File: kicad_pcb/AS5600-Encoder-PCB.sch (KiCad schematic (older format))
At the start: 12 parts, among them IC1 AS5600-ASOM, J1 Conn_01x04_Male, J2 Conn_01x04_Male

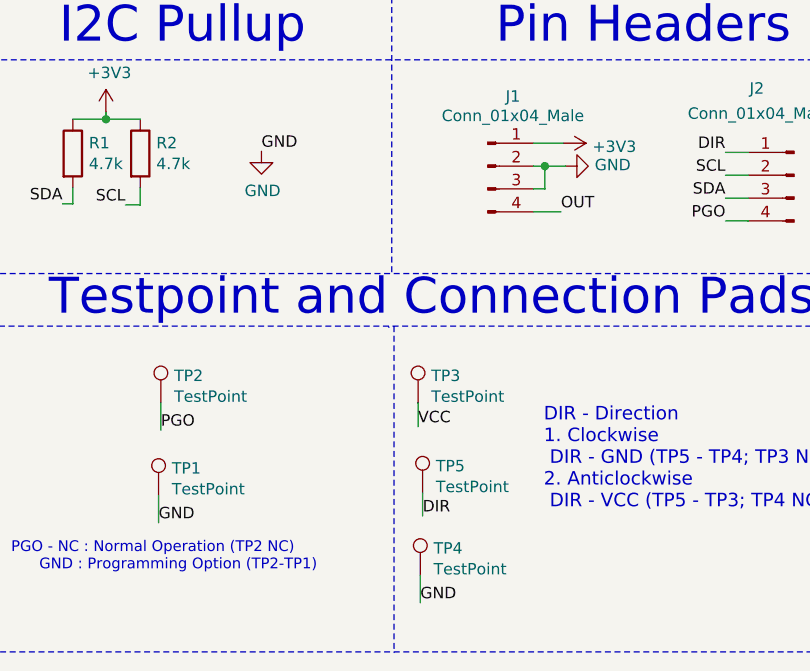
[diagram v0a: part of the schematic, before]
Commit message: Added SMD PCB for AS5600 Controller Board
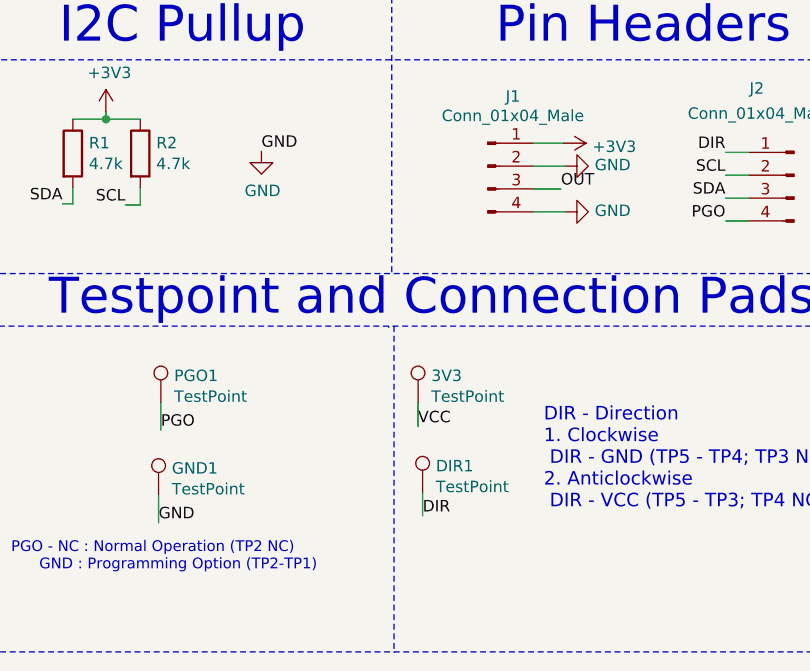
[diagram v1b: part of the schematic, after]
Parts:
- removed TP4: TestPoint, TestPoint:TestPoint_Pad_D2.5mm, symbol Connector:TestPoint
- C1: footprint Capacitor_THT:C_Disc_D5.0mm_W2.5mm_P5.00mm -> Capacitor_SMD:C_1206_3216Metric_Pad1.42x1.75mm_HandSolder
- C2: footprint Capacitor_THT:C_Radial_D6.3mm_H11.0mm_P2.50mm -> Capacitor_SMD:C_1206_3216Metric_Pad1.42x1.75mm_HandSolder
- R1, R2: footprint Resistor_THT:R_Axial_DIN0207_L6.3mm_D2.5mm_P10.16mm_Horizontal -> Resistor_SMD:R_1206_3216Metric_Pad1.42x1.75mm_HandSolder
- renumbered TP3 to 3V3, TP5 to DIR1, TP1 to GND1, TP2 to PGO1
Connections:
- net GND: now also J1.4 (Pin_4); no longer J1.3 (Pin_3)
- net OUT: now also J1.3 (Pin_3); no longer J1.4 (Pin_4)
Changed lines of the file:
@@
 F 0 "R1" H 3215 1246 50  0000 L CNN
 F 1 "4.7k" H 3215 1155 50  0000 L CNN
-F 2 "Resistor_THT:R_Axial_DIN0207_L6.3mm_D2.5mm_P10.16mm_Horizontal" V 3075 1200 50  0001 C CNN
+F 2 "Resistor_SMD:R_1206_3216Metric_Pad1.42x1.75mm_HandSolder" V 3075 1200 50  0001 C CNN
 F 3 "~" H 3145 1200 50  0001 C CNN
 	1    3145 1200
@@
 F 0 "R2" H 3510 1246 50  0000 L CNN
 F 1 "4.7k" H 3510 1155 50  0000 L CNN
-F 2 "Resistor_THT:R_Axial_DIN0207_L6.3mm_D2.5mm_P10.16mm_Horizontal" V 3370 1200 50  0001 C CNN
+F 2 "Resistor_SMD:R_1206_3216Metric_Pad1.42x1.75mm_HandSolder" V 3370 1200 50  0001 C CNN
 F 3 "~" H 3440 1200 50  0001 C CNN
 	1    3440 1200
@@
 F 0 "C1" H 885 2474 50  0000 R CNN
 F 1 "0.1uF" H 885 2565 50  0000 R CNN
-F 2 "Capacitor_THT:C_Disc_D5.0mm_W2.5mm_P5.00mm" H 1038 2370 50  0001 C CNN
+F 2 "Capacitor_SMD:C_1206_3216Metric_Pad1.42x1.75mm_HandSolder" H 1038 2370 50  0001 C CNN
 F 3 "~" H 1000 2520 50  0001 C CNN
 	1    1000 2520
@@
 F 0 "C2" H 1555 2566 50  0000 L CNN
 F 1 "10uF" H 1555 2475 50  0000 L CNN
-F 2 "Capacitor_THT:C_Radial_D6.3mm_H11.0mm_P2.50mm" H 1478 2370 50  0001 C CNN
+F 2 "Capacitor_SMD:C_1206_3216Metric_Pad1.42x1.75mm_HandSolder" H 1478 2370 50  0001 C CNN
 F 3 "~" H 1440 2520 50  0001 C CNN
 	1    1440 2520
@@
 	0    -1   -1   0
 $EndComp
-Text Label 5280 1455 0    50   ~ 0
+Text Label 5280 1355 0    50   ~ 0
 OUT
 $Comp
@@
 	5160 1155 5290 1155
 Wire Wire Line
-	5160 1455 5280 1455
-Wire Wire Line
-	5160 1255 5210 1255
-Wire Wire Line
-	5210 1255 5210 1355
-Wire Wire Line
-	5210 1355 5160 1355
-Wire Wire Line
-	5210 1255 5300 1255
-Connection ~ 5210 1255
-$Comp
-L Connector:TestPoint TP2
+	5160 1355 5280 1355
+$Comp
+L Connector:TestPoint PGO1
 U 1 1 61273AD3
 P 3530 2290
-F 0 "TP2" H 3588 2408 50  0000 L CNN
+F 0 "PGO1" H 3588 2408 50  0000 L CNN
 F 1 "TestPoint" H 3588 2317 50  0000 L CNN
 F 2 "TestPoint:TestPoint_Pad_D2.5mm" H 3730 2290 50  0001 C CNN
@@
 $EndComp
 $Comp
-L Connector:TestPoint TP3
+L Connector:TestPoint 3V3
 U 1 1 61274B3F
 P 4655 2290
-F 0 "TP3" H 4713 2408 50  0000 L CNN
+F 0 "3V3" H 4713 2408 50  0000 L CNN
 F 1 "TestPoint" H 4713 2317 50  0000 L CNN
 F 2 "TestPoint:TestPoint_Pad_D2.5mm" H 4855 2290 50  0001 C CNN
@@
 $EndComp
 $Comp
-L Connector:TestPoint TP5
+L Connector:TestPoint DIR1
 U 1 1 61275699
 P 4675 2685
-F 0 "TP5" H 4733 2803 50  0000 L CNN
+F 0 "DIR1" H 4733 2803 50  0000 L CNN
 F 1 "TestPoint" H 4733 2712 50  0000 L CNN
 F 2 "TestPoint:TestPoint_Pad_D2.5mm" H 4875 2685 50  0001 C CNN
 F 3 "~" H 4875 2685 50  0001 C CNN
 	1    4675 2685
-	1    0    0    -1
-$EndComp
-$Comp
-L Connector:TestPoint TP4
-U 1 1 61275D44
-P 4665 3045
-F 0 "TP4" H 4723 3163 50  0000 L CNN
-F 1 "TestPoint" H 4723 3072 50  0000 L CNN
-F 2 "TestPoint:TestPoint_Pad_D2.5mm" H 4865 3045 50  0001 C CNN
-F 3 "~" H 4865 3045 50  0001 C CNN
-	1    4665 3045
 	1    0    0    -1
 $EndComp
@@
 Text Label 1795 2370 0    50   ~ 0
 VCC
-Text Label 4665 3165 0    50   ~ 0
-GND
-Wire Wire Line
-	4665 3045 4665 3165
 Wire Wire Line
 	4675 2685 4675 2785
@@
 Text Notes 3040 1925 0    157  ~ 0
 Testpoint and Connection Pads
-$Comp
-L Connector:TestPoint TP1
-U 1 1 612B9A0F
-P 3520 2695
-F 0 "TP1" H 3578 2813 50  0000 L CNN
-F 1 "TestPoint" H 3578 2722 50  0000 L CNN
-F 2 "TestPoint:TestPoint_Pad_D2.5mm" H 3720 2695 50  0001 C CNN
-F 3 "~" H 3720 2695 50  0001 C CNN
-	1    3520 2695
-	1    0    0    -1
-$EndComp
-Text Label 3520 2815 0    50   ~ 0
-GND
-Wire Wire Line
-	3520 2695 3520 2815
 Text Notes 2875 3030 0    47   ~ 0
 PGO - NC : Normal Operation (TP2 NC)\n      GND : Programming Option (TP2-TP1)
@@
 Text Notes 5205 2760 0    59   ~ 0
 DIR - Direction\n1. Clockwise\n DIR - GND (TP5 - TP4; TP3 NC)\n2. Anticlockwise\n DIR - VCC (TP5 - TP3; TP4 NC)
+Wire Wire Line
+	5160 1255 5300 1255
+$Comp
+L power:GND #PWR0101
+U 1 1 6126228A
+P 5300 1455
+F 0 "#PWR0101" H 5300 1205 50  0001 C CNN
+F 1 "GND" V 5305 1327 50  0000 R CNN
+F 2 "" H 5300 1455 50  0001 C CNN
+F 3 "" H 5300 1455 50  0001 C CNN
+	1    5300 1455
+	0    -1   -1   0
+$EndComp
+Wire Wire Line
+	5160 1455 5300 1455
+Wire Wire Line
+	3520 2695 3520 2815
+Text Label 3520 2815 0    50   ~ 0
+GND
+$Comp
+L Connector:TestPoint GND1
+U 1 1 612B9A0F
+P 3520 2695
+F 0 "GND1" H 3578 2813 50  0000 L CNN
+F 1 "TestPoint" H 3578 2722 50  0000 L CNN
+F 2 "TestPoint:TestPoint_Pad_D2.5mm" H 3720 2695 50  0001 C CNN
+F 3 "~" H 3720 2695 50  0001 C CNN
+	1    3520 2695
+	1    0    0    -1
+$EndComp
 $EndSCHEMATC

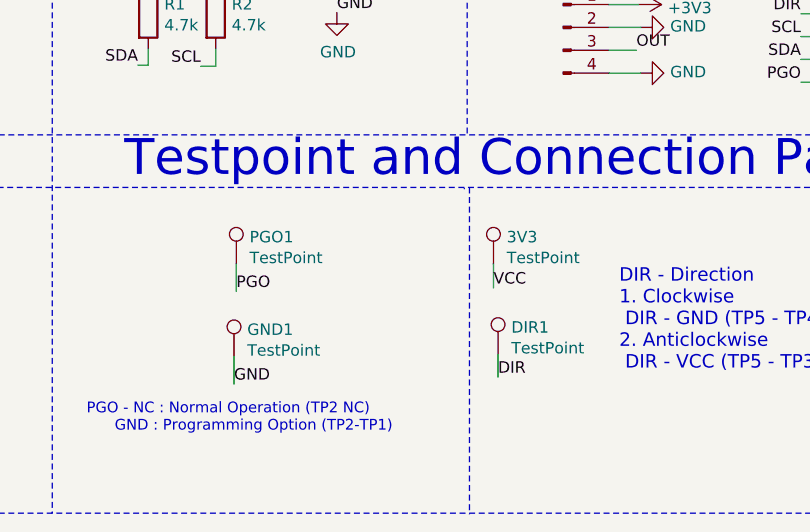
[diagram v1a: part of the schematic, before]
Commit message: Added Schematic asset
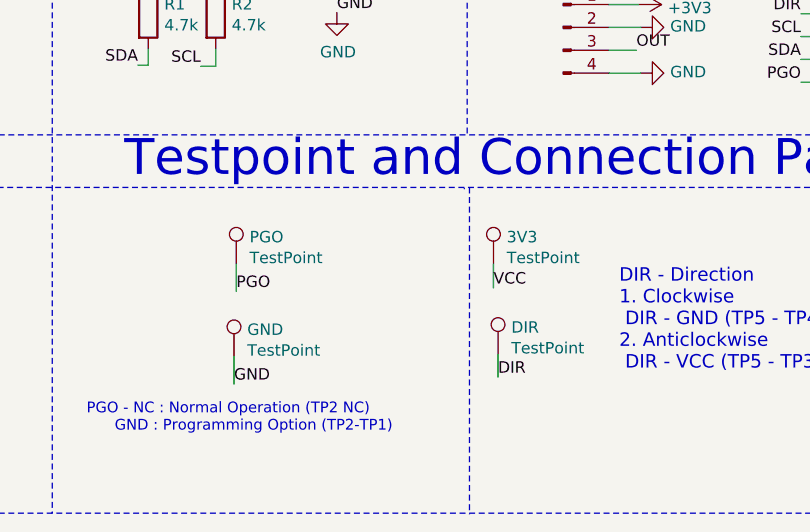
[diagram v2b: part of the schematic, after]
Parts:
- renumbered DIR1 to DIR, GND1 to GND, PGO1 to PGO
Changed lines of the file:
@@
 	5160 1355 5280 1355
 $Comp
-L Connector:TestPoint PGO1
+L Connector:TestPoint PGO
 U 1 1 61273AD3
 P 3530 2290
-F 0 "PGO1" H 3588 2408 50  0000 L CNN
+F 0 "PGO" H 3588 2408 50  0000 L CNN
 F 1 "TestPoint" H 3588 2317 50  0000 L CNN
 F 2 "TestPoint:TestPoint_Pad_D2.5mm" H 3730 2290 50  0001 C CNN
@@
 $EndComp
 $Comp
-L Connector:TestPoint DIR1
+L Connector:TestPoint DIR
 U 1 1 61275699
 P 4675 2685
-F 0 "DIR1" H 4733 2803 50  0000 L CNN
+F 0 "DIR" H 4733 2803 50  0000 L CNN
 F 1 "TestPoint" H 4733 2712 50  0000 L CNN
 F 2 "TestPoint:TestPoint_Pad_D2.5mm" H 4875 2685 50  0001 C CNN
@@
 Wire Notes Line
 	6805 475  6805 3380
-Text Notes 660  715  0    157  ~ 0
-AS5600 Encoder
 Text Notes 3085 735  0    157  ~ 0
 I2C Pullup
@@
 GND
 $Comp
-L Connector:TestPoint GND1
+L Connector:TestPoint GND
 U 1 1 612B9A0F
 P 3520 2695
-F 0 "GND1" H 3578 2813 50  0000 L CNN
+F 0 "GND" H 3578 2813 50  0000 L CNN
 F 1 "TestPoint" H 3578 2722 50  0000 L CNN
 F 2 "TestPoint:TestPoint_Pad_D2.5mm" H 3720 2695 50  0001 C CNN
@@
 	1    0    0    -1
 $EndComp
+Text Notes 660  715  0    157  ~ 0
+AS5600 Encoder
 $EndSCHEMATC

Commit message: Made suggested changes
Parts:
- R1, R2: footprint Resistor_SMD:R_1206_3216Metric_Pad1.42x1.75mm_HandSolder -> Resistor_SMD:R_0603_1608Metric_Pad1.05x0.95mm_HandSolder
- renumbered DIR to DIR1, GND to GND1, PGO to PGO1
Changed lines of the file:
@@
 F 0 "R1" H 3215 1246 50  0000 L CNN
 F 1 "4.7k" H 3215 1155 50  0000 L CNN
-F 2 "Resistor_SMD:R_1206_3216Metric_Pad1.42x1.75mm_HandSolder" V 3075 1200 50  0001 C CNN
+F 2 "Resistor_SMD:R_0603_1608Metric_Pad1.05x0.95mm_HandSolder" V 3075 1200 50  0001 C CNN
 F 3 "~" H 3145 1200 50  0001 C CNN
 	1    3145 1200
@@
 F 0 "R2" H 3510 1246 50  0000 L CNN
 F 1 "4.7k" H 3510 1155 50  0000 L CNN
-F 2 "Resistor_SMD:R_1206_3216Metric_Pad1.42x1.75mm_HandSolder" V 3370 1200 50  0001 C CNN
+F 2 "Resistor_SMD:R_0603_1608Metric_Pad1.05x0.95mm_HandSolder" V 3370 1200 50  0001 C CNN
 F 3 "~" H 3440 1200 50  0001 C CNN
 	1    3440 1200
@@
 	5160 1355 5280 1355
 $Comp
-L Connector:TestPoint PGO
+L Connector:TestPoint PGO1
 U 1 1 61273AD3
 P 3530 2290
-F 0 "PGO" H 3588 2408 50  0000 L CNN
+F 0 "PGO1" H 3588 2408 50  0000 L CNN
 F 1 "TestPoint" H 3588 2317 50  0000 L CNN
 F 2 "TestPoint:TestPoint_Pad_D2.5mm" H 3730 2290 50  0001 C CNN
@@
 $EndComp
 $Comp
-L Connector:TestPoint DIR
+L Connector:TestPoint DIR1
 U 1 1 61275699
 P 4675 2685
-F 0 "DIR" H 4733 2803 50  0000 L CNN
+F 0 "DIR1" H 4733 2803 50  0000 L CNN
 F 1 "TestPoint" H 4733 2712 50  0000 L CNN
 F 2 "TestPoint:TestPoint_Pad_D2.5mm" H 4875 2685 50  0001 C CNN
@@
 GND
 $Comp
-L Connector:TestPoint GND
+L Connector:TestPoint GND1
 U 1 1 612B9A0F
 P 3520 2695
-F 0 "GND" H 3578 2813 50  0000 L CNN
+F 0 "GND1" H 3578 2813 50  0000 L CNN
 F 1 "TestPoint" H 3578 2722 50  0000 L CNN
 F 2 "TestPoint:TestPoint_Pad_D2.5mm" H 3720 2695 50  0001 C CNN
